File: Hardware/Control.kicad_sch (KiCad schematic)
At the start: 45 parts, among them J1 DM3AT-SF-PEJM5, SW1 PTS_647_SN50_SMTR2_LFS, SW2 PTS_647_SN50_SMTR2_LFS, SW3 PTS_647_SN50_SMTR2_LFS, U1 RP2354B, X2 ABM8-272-T3

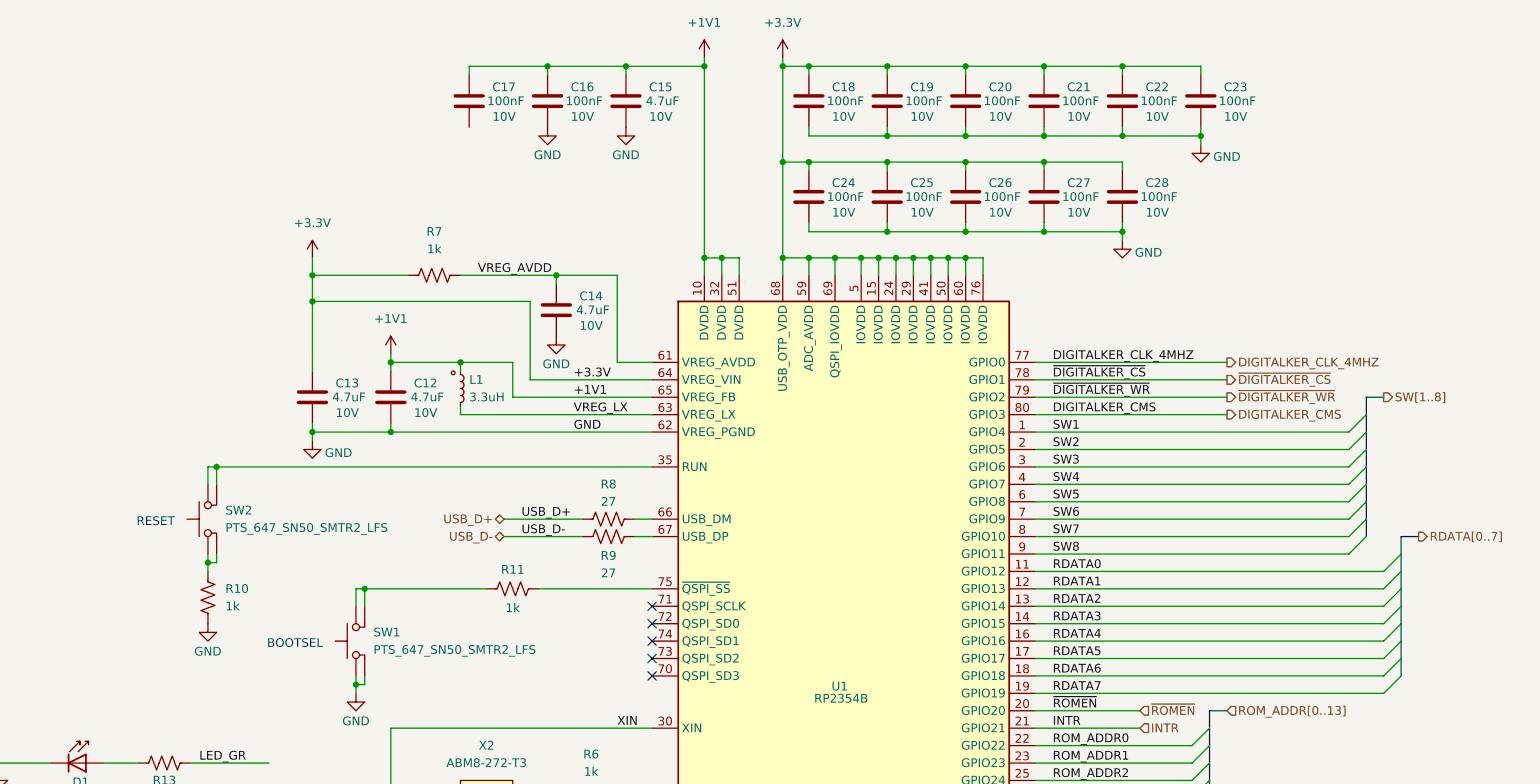
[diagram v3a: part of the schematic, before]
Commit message: RP2354 placement
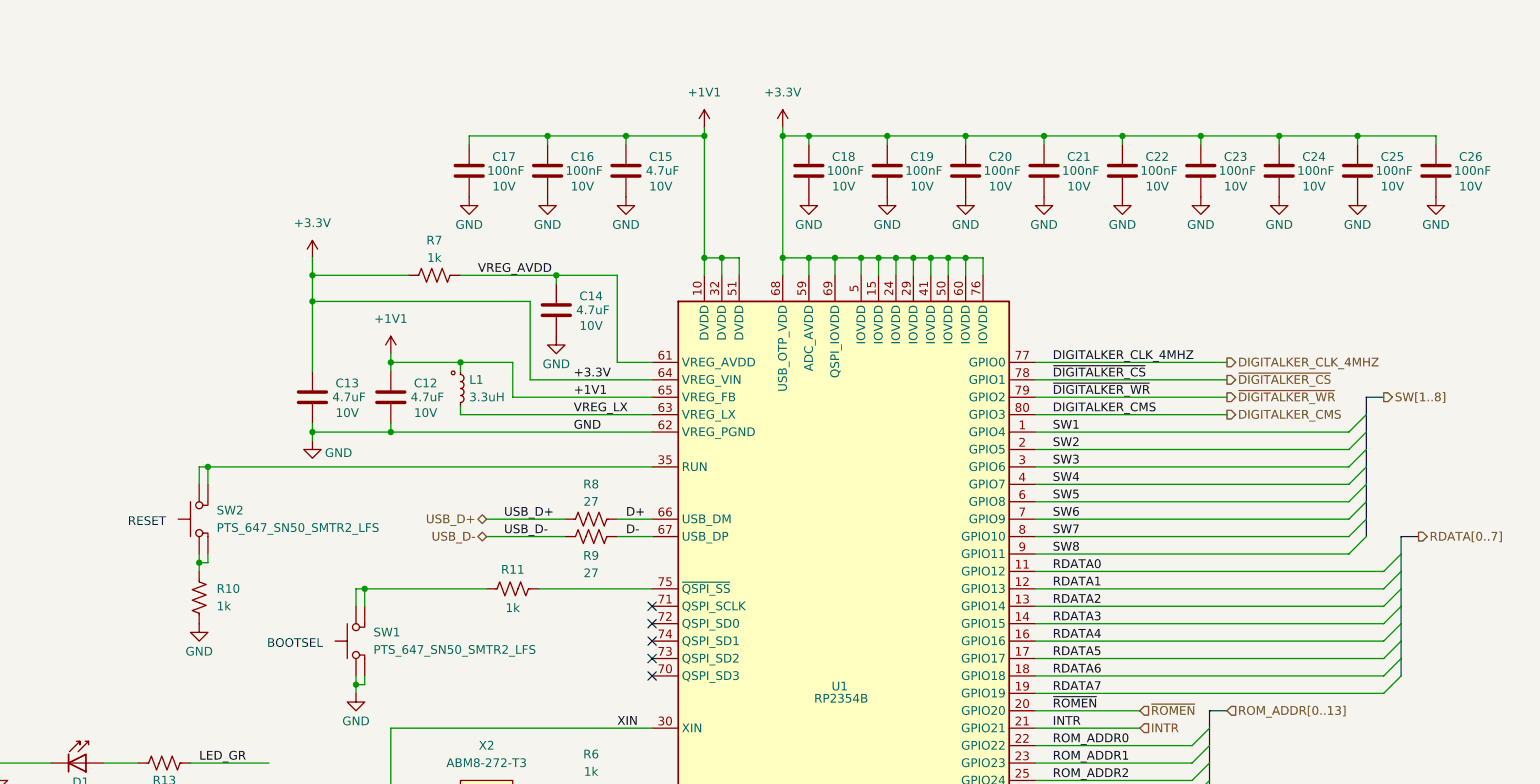
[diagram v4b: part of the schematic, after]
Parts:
- removed C27, C28: 100nF, Capacitor_SMD:C_0402_1005Metric, symbol Device:C
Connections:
- net GND: now also C17.2
- net D-: now reaches R9.1, U1.67 (USB_DP)
- net D+: now reaches R8.1, U1.66 (USB_DM)
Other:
- moved on the sheet: C15, C16, C17, C18, C19, C20, C21, C22, C23, R10, R8, R9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

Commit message: layout complete
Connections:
- net BCLK: now also U1.46 (GPIO37); no longer U1.47 (GPIO38)
- net FSYNC: now also U1.45 (GPIO36); no longer U1.46 (GPIO37)
- net INTR: now also U1.44 (GPIO35); no longer U1.21 (GPIO21)
- net ROM_ADDR0: now also U1.20 (GPIO20); no longer U1.22 (GPIO22)
- net ROM_ADDR1: now also U1.21 (GPIO21); no longer U1.23 (GPIO23)
- net ROM_ADDR10: now also U1.38 (GPIO30); no longer U1.40 (GPIO32)
- net ROM_ADDR11: now also U1.39 (GPIO31); no longer U1.42 (GPIO33)
- net ROM_ADDR12: now also U1.40 (GPIO32); no longer U1.43 (GPIO34)
- net ROM_ADDR13: now also U1.42 (GPIO33); no longer U1.44 (GPIO35)
- net ROM_ADDR2: now also U1.22 (GPIO22); no longer U1.25 (GPIO24)
- net ROM_ADDR3: now also U1.23 (GPIO23); no longer U1.26 (GPIO25)
- net ROM_ADDR4: now also U1.25 (GPIO24); no longer U1.27 (GPIO26)
- net ROM_ADDR5: now also U1.26 (GPIO25); no longer U1.28 (GPIO27)
- net ROM_ADDR6: now also U1.27 (GPIO26); no longer U1.36 (GPIO28)
- net ROM_ADDR7: now also U1.28 (GPIO27); no longer U1.37 (GPIO29)
- net ROM_ADDR8: now also U1.36 (GPIO28); no longer U1.38 (GPIO30)
- net ROM_ADDR9: now also U1.37 (GPIO29); no longer U1.39 (GPIO31)
- net SDATA: now also U1.47 (GPIO38); no longer U1.45 (GPIO36)
- net ~{ROMEN}: now also U1.43 (GPIO34); no longer U1.20 (GPIO20)

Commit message: swap D2 to amber, silk text
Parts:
- D2: value 150060RS75000 -> 150060AS75000; Color RED -> AMBER; MPN 150060RS75000 -> 150060AS75000
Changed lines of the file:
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@@
 			)
 		)
-		(property "Value" "150060RS75000"
+		(property "Value" "150060AS75000"
 			(at 104.648 162.814 0)
 			(show_name no)
@@
 			)
 		)
-		(property "Datasheet" "https://www.we-online.com/components/products/datasheet/150060RS75000.pdf"
+		(property "Datasheet" "https://www.we-online.com/components/products/datasheet/150060AS75000.pdf"
 			(at 104.14 157.48 0)
 			(hide yes)
@@
 			)
 		)
-		(property "Description" "LED RED CLEAR 0603 SMD"
+		(property "Description" "LED AMBER CLEAR 0603 SMD"
 			(at 105.41 157.48 0)
 			(hide yes)
@@
 			)
 		)
-		(property "Color" "RED"
+		(property "Color" "AMBER"
 			(at 104.648 164.846 0)
 			(show_name no)
@@
 			)
 		)
-		(property "MPN" "150060RS75000"
+		(property "MPN" "150060AS75000"
 			(at 105.41 157.48 0)
 			(hide yes)

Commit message: generate outputs
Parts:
- C10, C11: JLCPCB Part # (none) -> C106997
- C12, C13, C14, C15: JLCPCB Part # (none) -> C318563; MPN CL05A475MP5NRNC -> CL05A475MO5NUNC; Voltage 10V -> 25V
- C16, C17, C18, C19, C20, C21, C22, C23, C24, C25, C26, C29, C30: JLCPCB Part # (none) -> C105883; MPN GRM155R71A104KA01D -> CC0402KRX7R8BB104; Voltage 10V -> 25V
- C48: JLCPCB Part # (none) -> C315248; MPN CL05A106MQ5NUNC -> CL05A106MP5NUNC
- D1: JLCPCB Part # (none) -> C6848499
- D2: JLCPCB Part # (none) -> C6976659
- J1: JLCPCB Part # (none) -> C114218
- L1: JLCPCB Part # (none) -> C42411119
- R10, R11, R6, R7: JLCPCB Part # (none) -> C105637
- R12, R28, R29, R30, R31, R32: JLCPCB Part # (none) -> C60490
- R13, R33: JLCPCB Part # (none) -> C327373
- R8, R9: JLCPCB Part # (none) -> C138021
- SW1, SW2, SW3: JLCPCB Part # (none) -> C2799414
- U1: JLCPCB Part # (none) -> C39843328
- X2: JLCPCB Part # (none) -> C20625731
